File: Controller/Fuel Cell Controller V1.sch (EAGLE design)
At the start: 114 parts, among them IC1 4081D, M1 MOSFETBOARD, T1 TEENSY_3.1_ALL_PINS, U1 SN74ALS153D, U2 MAX3221CPWR, U3 ATMEGA328P_TQFP, U4 ATMEGA328P_TQFP, U5 MAX3221CPWR, U6 ATMEGA328P_TQFP

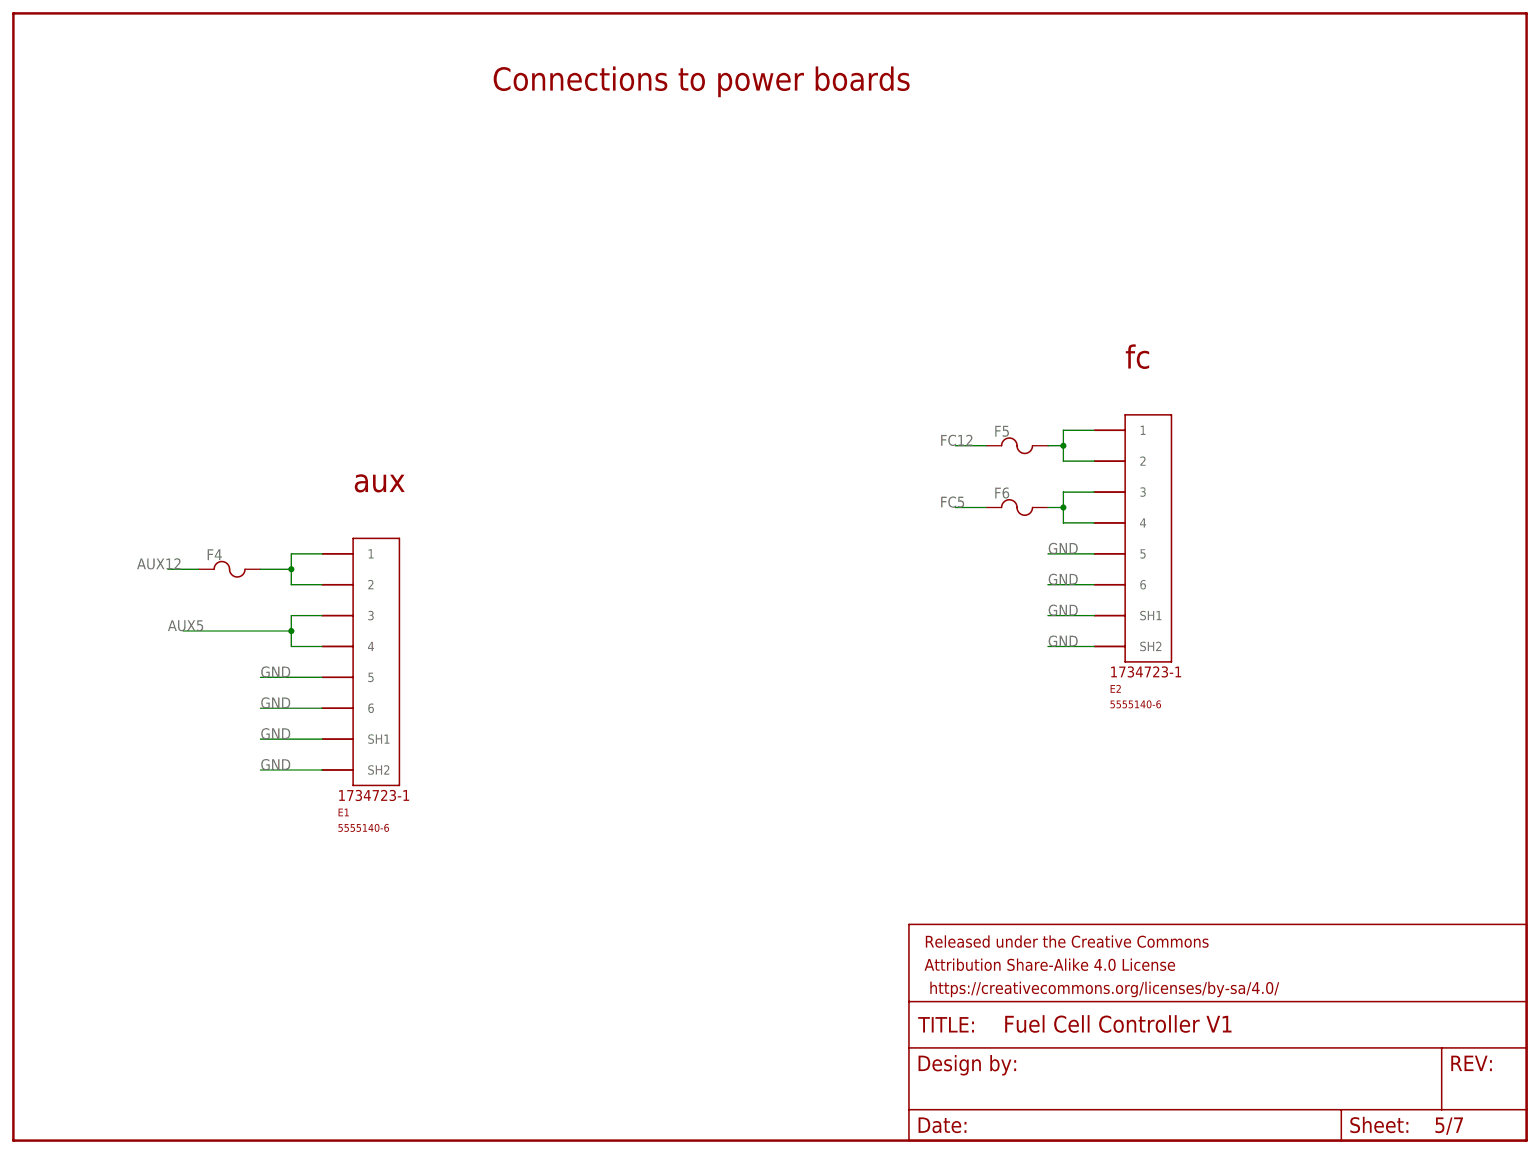
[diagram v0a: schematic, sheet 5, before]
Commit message: added ground vias, making silk screen nice, starting documentation
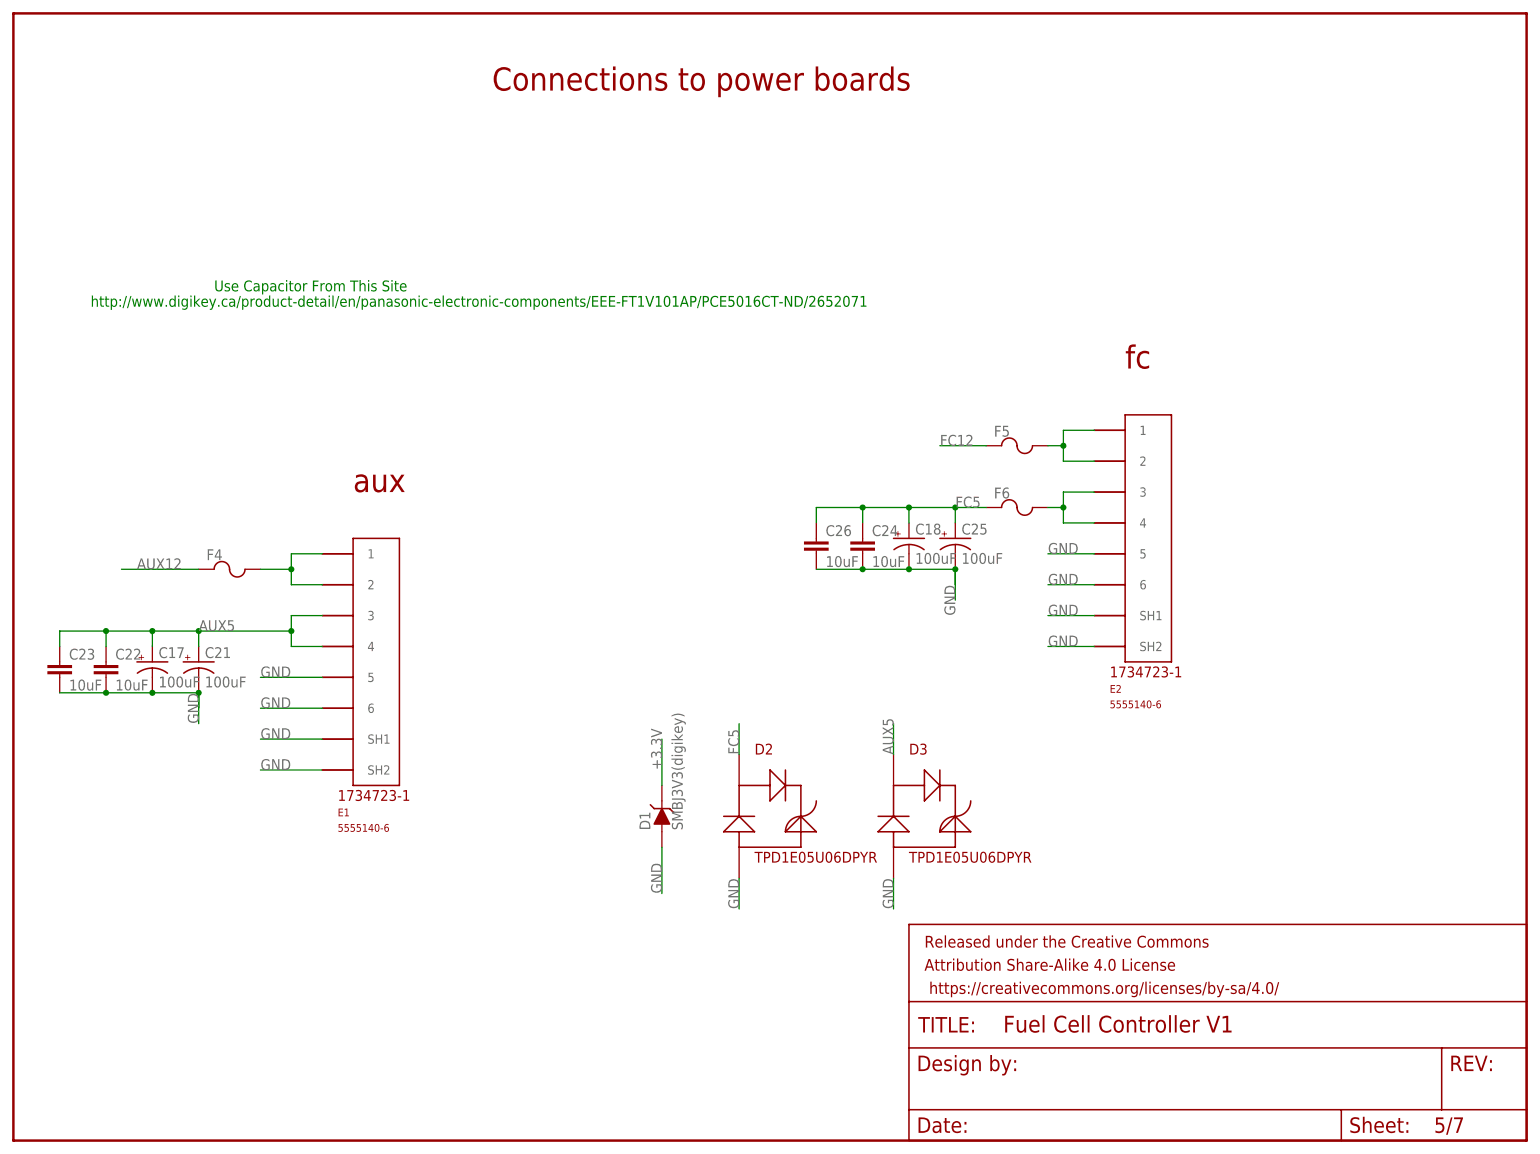
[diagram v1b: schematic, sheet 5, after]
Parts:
- added C17, C18, C21, C25: 100uF, SparkFun-Capacitors:CAP_POLD
- added C22, C23, C24, C26: 10uF, SparkFun-Capacitors-extra:CAP0805
- added D1: SMBJ3V3(digikey), bt_diode:5KASMC
- added D2, D3: TPD1E05U06DPYR, TPD1E05U06DPYR:TPD1E05U06DPYR
- added STANDOFF1, STANDOFF2, STANDOFF3, STANDOFF4, STANDOFF5: STAND-OFF, SparkFun-Electromechanical:STAND-OFF
- added U$1: TRUMP, trump:TRUMP
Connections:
- net +3.3V: now also D1.C
- net AUX5: now also C17.+, C21.+, C22.1, C23.1, D3.P$1
- net FC5: now also C18.+, C24.1, C25.+, C26.1, D2.P$1
- net GND: now also C17.-, C18.-, C21.-, C22.2, C23.2, C24.2, C25.-, C26.2, D1.A, D2.P$2, D3.P$2
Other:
- note added: "Use Capacitor From This Site"
- note added: "http://www.digikey.ca/product-detail/en/panasonic-electronic-components/EEE-FT1V101AP/PCE5016CT-ND/2652071"
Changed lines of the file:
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@@
 <part name="R33" library="adafruit" deviceset="R-US_" device="R0603" value="100"/>
 <part name="R34" library="adafruit" deviceset="R-US_" device="R0603" value="100"/>
+<part name="STANDOFF1" library="SparkFun-Electromechanical" deviceset="STAND-OFF" device=""/>
+<part name="STANDOFF2" library="SparkFun-Electromechanical" deviceset="STAND-OFF" device=""/>
+<part name="STANDOFF3" library="SparkFun-Electromechanical" deviceset="STAND-OFF" device=""/>
+<part name="STANDOFF4" library="SparkFun-Electromechanical" deviceset="STAND-OFF" device=""/>
+<part name="STANDOFF5" library="SparkFun-Electromechanical" deviceset="STAND-OFF" device=""/>
+<part name="C21" library="SparkFun-Capacitors" deviceset="CAP_POL" device="D" value="100uF"/>
+<part name="C25" library="SparkFun-Capacitors" deviceset="CAP_POL" device="D" value="100uF"/>
+<part name="C17" library="SparkFun-Capacitors" deviceset="CAP_POL" device="D" value="100uF"/>
+<part name="C18" library="SparkFun-Capacitors" deviceset="CAP_POL" device="D" value="100uF"/>
+<part name="C22" library="SparkFun-Capacitors-extra" deviceset="CAP" device="0805" value="10uF"/>
+<part name="C23" library="SparkFun-Capacitors-extra" deviceset="CAP" device="0805" value="10uF"/>
+<part name="C24" library="SparkFun-Capacitors-extra" deviceset="CAP" device="0805" value="10uF"/>
+<part name="C26" library="SparkFun-Capacitors-extra" deviceset="CAP" device="0805" value="10uF"/>
+<part name="D1" library="bt_diode" deviceset="5KA" device="SMC" value="SMBJ3V3(digikey)"/>
+<part name="D2" library="TPD1E05U06DPYR" deviceset="TPD1E05U06DPYR" device=""/>
+<part name="D3" library="TPD1E05U06DPYR" deviceset="TPD1E05U06DPYR" device=""/>
+<part name="U$1" library="trump" deviceset="TRUMP" device=""/>
 </parts>
 <sheets>
@@
 <instance part="R3" gate="G$1" x="139.7" y="109.22" rot="R90"/>
 <instance part="R4" gate="G$1" x="147.32" y="109.22" rot="R90"/>
+<instance part="STANDOFF1" gate="G$1" x="172.72" y="45.72"/>
+<instance part="STANDOFF2" gate="G$1" x="180.34" y="45.72"/>
+<instance part="STANDOFF3" gate="G$1" x="187.96" y="45.72"/>
+<instance part="STANDOFF4" gate="G$1" x="195.58" y="45.72"/>
+<instance part="STANDOFF5" gate="G$1" x="203.2" y="45.72"/>
 </instances>
 <busses>
@@
 <text x="55.88" y="106.68" size="3.81" layer="94">aux</text>
 <text x="182.88" y="127" size="3.81" layer="94">fc</text>
+<text x="33.02" y="139.7" size="1.778" layer="91">Use Capacitor From This Site</text>
+<text x="12.7" y="137.16" size="1.778" layer="91">http://www.digikey.ca/product-detail/en/panasonic-electronic-components/EEE-FT1V101AP/PCE5016CT-ND/2652071</text>
 </plain>
 <instances>
@@
 <instance part="F5" gate="G$1" x="165.1" y="114.3"/>
 <instance part="F6" gate="G$1" x="165.1" y="104.14"/>
+<instance part="C21" gate="G$1" x="30.48" y="78.74"/>
+<instance part="C25" gate="G$1" x="154.94" y="99.06"/>
+<instance part="C17" gate="G$1" x="22.86" y="78.74"/>
+<instance part="C18" gate="G$1" x="147.32" y="99.06"/>
+<instance part="C22" gate="G$1" x="15.24" y="76.2"/>
+<instance part="C23" gate="G$1" x="7.62" y="76.2"/>
+<instance part="C24" gate="G$1" x="139.7" y="96.52"/>
+<instance part="C26" gate="G$1" x="132.08" y="96.52"/>
+<instance part="D1" gate="D1" x="106.68" y="53.34" rot="R90"/>
+<instance part="D2" gate="G$1" x="119.38" y="53.34"/>
+<instance part="D3" gate="G$1" x="144.78" y="53.34"/>
+<instance part="U$1" gate="G$1" x="5.08" y="5.08"/>
 </instances>
 <busses>
@@
 <wire x1="177.8" y1="81.28" x2="170.18" y2="81.28" width="0.1524" layer="91"/>
 <label x="170.18" y="81.28" size="1.778" layer="95"/>
+</segment>
+<segment>
+<pinref part="C25" gate="G$1" pin="-"/>
+<wire x1="154.94" y1="91.44" x2="154.94" y2="93.98" width="0.1524" layer="91"/>
+<wire x1="154.94" y1="93.98" x2="154.94" y2="88.9" width="0.1524" layer="91"/>
+<label x="154.94" y="86.36" size="1.778" layer="95" rot="R90"/>
+<pinref part="C18" gate="G$1" pin="-"/>
+<wire x1="147.32" y1="93.98" x2="154.94" y2="93.98" width="0.1524" layer="91"/>
+<junction x="154.94" y="93.98"/>
+<pinref part="C26" gate="G$1" pin="2"/>
+<pinref part="C24" gate="G$1" pin="2"/>
+<wire x1="132.08" y1="93.98" x2="139.7" y2="93.98" width="0.1524" layer="91"/>
+<wire x1="139.7" y1="93.98" x2="147.32" y2="93.98" width="0.1524" layer="91"/>
+<junction x="139.7" y="93.98"/>
+<junction x="147.32" y="93.98"/>
+</segment>
+<segment>
+<pinref part="C21" gate="G$1" pin="-"/>
+<wire x1="30.48" y1="71.12" x2="30.48" y2="73.66" width="0.1524" layer="91"/>
+<wire x1="30.48" y1="73.66" x2="30.48" y2="68.58" width="0.1524" layer="91"/>
+<label x="30.48" y="68.58" size="1.778" layer="95" rot="R90"/>
+<pinref part="C17" gate="G$1" pin="-"/>
+<wire x1="22.86" y1="73.66" x2="30.48" y2="73.66" width="0.1524" layer="91"/>
+<junction x="30.48" y="73.66"/>
+<pinref part="C22" gate="G$1" pin="2"/>
+<wire x1="22.86" y1="73.66" x2="15.24" y2="73.66" width="0.1524" layer="91"/>
+<junction x="22.86" y="73.66"/>
+<pinref part="C23" gate="G$1" pin="2"/>
+<wire x1="15.24" y1="73.66" x2="7.62" y2="73.66" width="0.1524" layer="91"/>
+<junction x="15.24" y="73.66"/>
+</segment>
+<segment>
+<pinref part="D1" gate="D1" pin="A"/>
+<wire x1="106.68" y1="48.26" x2="106.68" y2="40.64" width="0.1524" layer="91"/>
+<label x="106.68" y="40.64" size="1.778" layer="95" rot="R90"/>
+</segment>
+<segment>
+<pinref part="D2" gate="G$1" pin="P$2"/>
+<wire x1="119.38" y1="43.18" x2="119.38" y2="38.1" width="0.1524" layer="91"/>
+<label x="119.38" y="38.1" size="1.778" layer="95" rot="R90"/>
+</segment>
+<segment>
+<pinref part="D3" gate="G$1" pin="P$2"/>
+<wire x1="144.78" y1="43.18" x2="144.78" y2="38.1" width="0.1524" layer="91"/>
+<label x="144.78" y="38.1" size="1.778" layer="95" rot="R90"/>
 </segment>
 </net>
@@
 <segment>
 <pinref part="F4" gate="G$1" pin="1"/>
-<wire x1="30.48" y1="93.98" x2="25.4" y2="93.98" width="0.1524" layer="91"/>
 <label x="20.32" y="93.98" size="1.778" layer="95"/>
+<wire x1="30.48" y1="93.98" x2="17.78" y2="93.98" width="0.1524" layer="91"/>
 </segment>
 </net>
 <net name="AUX5" class="0">
 <segment>
-<label x="25.4" y="83.82" size="1.778" layer="95"/>
+<label x="30.48" y="83.82" size="1.778" layer="95"/>
 <pinref part="E1" gate="G$1" pin="4"/>
 <wire x1="50.8" y1="81.28" x2="45.72" y2="81.28" width="0.1524" layer="91"/>
@@
 <wire x1="45.72" y1="86.36" x2="50.8" y2="86.36" width="0.1524" layer="91"/>
 <junction x="45.72" y="83.82"/>
-<wire x1="27.94" y1="83.82" x2="45.72" y2="83.82" width="0.1524" layer="91"/>
+<pinref part="C21" gate="G$1" pin="+"/>
+<wire x1="30.48" y1="83.82" x2="45.72" y2="83.82" width="0.1524" layer="91"/>
+<wire x1="30.48" y1="81.28" x2="30.48" y2="83.82" width="0.1524" layer="91"/>
+<pinref part="C17" gate="G$1" pin="+"/>
+<wire x1="30.48" y1="83.82" x2="22.86" y2="83.82" width="0.1524" layer="91"/>
+<wire x1="22.86" y1="83.82" x2="22.86" y2="81.28" width="0.1524" layer="91"/>
+<junction x="30.48" y="83.82"/>
+<pinref part="C23" gate="G$1" pin="1"/>
+<wire x1="7.62" y1="81.28" x2="7.62" y2="83.82" width="0.1524" layer="91"/>
+<wire x1="7.62" y1="83.82" x2="15.24" y2="83.82" width="0.1524" layer="91"/>
+<junction x="22.86" y="83.82"/>
+<pinref part="C22" gate="G$1" pin="1"/>
+<wire x1="15.24" y1="83.82" x2="22.86" y2="83.82" width="0.1524" layer="91"/>
+<wire x1="15.24" y1="81.28" x2="15.24" y2="83.82" width="0.1524" layer="91"/>
+<junction x="15.24" y="83.82"/>
+</segment>
+<segment>
+<pinref part="D3" gate="G$1" pin="P$1"/>
+<wire x1="144.78" y1="63.5" x2="144.78" y2="68.58" width="0.1524" layer="91"/>
+<label x="144.78" y="63.5" size="1.778" layer="95" rot="R90"/>
 </segment>
 </net>
@@
 <segment>
 <pinref part="F5" gate="G$1" pin="1"/>
-<wire x1="160.02" y1="114.3" x2="154.94" y2="114.3" width="0.1524" layer="91"/>
 <label x="152.4" y="114.3" size="1.778" layer="95"/>
+<wire x1="160.02" y1="114.3" x2="152.4" y2="114.3" width="0.1524" layer="91"/>
 </segment>
 </net>
@@
 <segment>
 <pinref part="F6" gate="G$1" pin="1"/>
-<wire x1="160.02" y1="104.14" x2="154.94" y2="104.14" width="0.1524" layer="91"/>
-<label x="152.4" y="104.14" size="1.778" layer="95"/>
-</segment>
-</net>
+<label x="154.94" y="104.14" size="1.778" layer="95"/>
+<pinref part="C25" gate="G$1" pin="+"/>
+<wire x1="154.94" y1="104.14" x2="160.02" y2="104.14" width="0.1524" layer="91"/>
+<wire x1="154.94" y1="101.6" x2="154.94" y2="104.14" width="0.1524" layer="91"/>
+<pinref part="C18" gate="G$1" pin="+"/>
+<wire x1="154.94" y1="104.14" x2="147.32" y2="104.14" width="0.1524" layer="91"/>
+<wire x1="147.32" y1="104.14" x2="147.32" y2="101.6" width="0.1524" layer="91"/>
+<junction x="154.94" y="104.14"/>
+<pinref part="C26" gate="G$1" pin="1"/>
+<wire x1="132.08" y1="101.6" x2="132.08" y2="104.14" width="0.1524" layer="91"/>
+<wire x1="132.08" y1="104.14" x2="139.7" y2="104.14" width="0.1524" layer="91"/>
+<junction x="147.32" y="104.14"/>
+<pinref part="C24" gate="G$1" pin="1"/>
+<wire x1="139.7" y1="104.14" x2="147.32" y2="104.14" width="0.1524" layer="91"/>
+<wire x1="139.7" y1="101.6" x2="139.7" y2="104.14" width="0.1524" layer="91"/>
+<junction x="139.7" y="104.14"/>
+</segment>
+<segment>
+<pinref part="D2" gate="G$1" pin="P$1"/>
+<wire x1="119.38" y1="63.5" x2="119.38" y2="68.58" width="0.1524" layer="91"/>
+<label x="119.38" y="63.5" size="1.778" layer="95" rot="R90"/>
+</segment>
+</net>
+<net name="+3.3V" class="0">
+<segment>
+<pinref part="D1" gate="D1" pin="C"/>
+<wire x1="106.68" y1="58.42" x2="106.68" y2="66.04" width="0.1524" layer="91"/>
+<label x="106.68" y="60.96" size="1.778" layer="95" rot="R90"/>
+</segment>
+</net>
